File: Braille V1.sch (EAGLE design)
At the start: 85 parts, among them IC1 TD62083, IC2 74HC238D, IC3 74HC238D, IC4 TD62083, IC5 74HC238D, IC6 74HC238D, J1 POWER_JACKSLT, Q1 TBD62783AFG,EL, Q2 TBD62783AFG,EL, U2 LM317

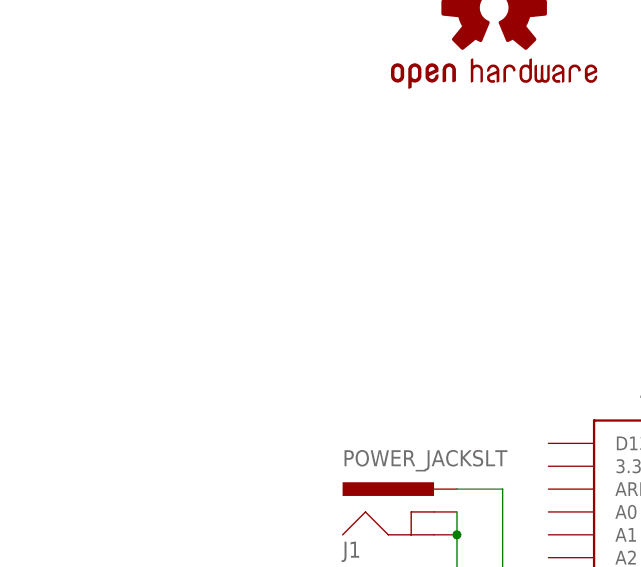
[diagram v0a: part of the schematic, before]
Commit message: Updated Test Point
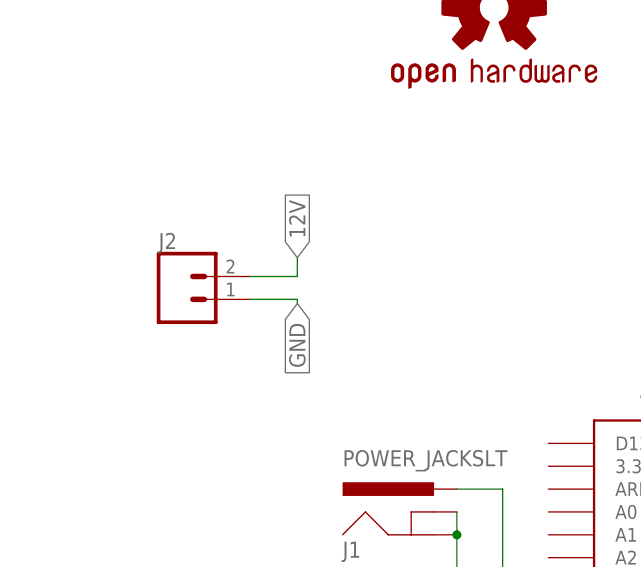
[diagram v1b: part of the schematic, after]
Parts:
- added J2: (no value), SparkFun-Connectors:CONN_02
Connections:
- net 12V: now also J2.2
- net GND: now also J2.1
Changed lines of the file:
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@@
 <setting verticaltext="up"/>
 </settings>
-<grid distance="0.001" unitdist="inch" unit="inch" style="lines" multiple="1" display="no" altdistance="0.01" altunitdist="inch" altunit="inch"/>
+<grid distance="0.1" unitdist="inch" unit="inch" style="lines" multiple="1" display="no" altdistance="0.01" altunitdist="inch" altunit="inch"/>
 <layers>
 <layer number="1" name="Top" color="4" fill="1" visible="no" active="no"/>
@@
 <part name="J3" library="SparkFun-Connectors" deviceset="CONN_02" device=""/>
 <part name="LOGO1" library="SparkFun-Aesthetics" deviceset="OSHW-LOGO" device="L-COPPER"/>
+<part name="J2" library="SparkFun-Connectors" deviceset="CONN_02" device=""/>
 </parts>
 <sheets>
@@
 </instance>
 <instance part="LOGO1" gate="G$1" x="-242.2906" y="159.8676" smashed="yes"/>
+<instance part="J2" gate="G$1" x="-277.0378" y="127.4572" smashed="yes">
+<attribute name="VALUE" x="-279.5778" y="122.6312" size="1.778" layer="96" font="vector"/>
+<attribute name="NAME" x="-279.5778" y="133.0452" size="1.778" layer="95" font="vector"/>
+</instance>
 </instances>
 <busses>
@@
 <wire x1="-238.1622" y1="22.085296875" x2="-228.940359375" y2="22.085296875" width="0.1524" layer="91"/>
 <junction x="-228.940359375" y="22.085296875"/>
+</segment>
+<segment>
+<pinref part="J2" gate="G$1" pin="1"/>
+<wire x1="-269.4178" y1="127.4572" x2="-264.16" y2="127.4572" width="0.1524" layer="91"/>
+<wire x1="-264.16" y1="127.4572" x2="-264.16" y2="127" width="0.1524" layer="91"/>
+<label x="-264.16" y="127" size="1.778" layer="95" rot="R270" xref="yes"/>
 </segment>
 </net>
@@
 <label x="-281.8384" y="71.12" size="2.54" layer="95" rot="R180" xref="yes"/>
 </segment>
-</net>
+<segment>
+<pinref part="J2" gate="G$1" pin="2"/>
+<wire x1="-269.4178" y1="129.9972" x2="-264.16" y2="129.9972" width="0.1524" layer="91"/>
+<wire x1="-264.16" y1="129.9972" x2="-264.16" y2="132.08" width="0.1524" layer="91"/>
+<label x="-264.16" y="132.08" size="1.778" layer="95" rot="R90" xref="yes"/>
+</segment>
+</net>
